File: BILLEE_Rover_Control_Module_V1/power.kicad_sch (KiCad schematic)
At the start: 76 parts, among them CN2 XT60PW-M, U10 +22.2V_POE_POWER, U2 TPS1HA08BQPWPRQ1, U20 +12V_NET_SW_PWR, U23 TPS1HA08BQPWPRQ1, U24 LT8612EUDE#TRPBF, U25 +12V_AUX_PWR, U38 MCP9808T-E/MS, U5 TPS1HA08BQPWPRQ1, U6 INA780BIDEKR, U7 LT8612EUDE#TRPBF, U8 LT8612EUDE#TRPBF, U9 +20V_JETSON_PWR

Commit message: more goodies
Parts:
- removed CN2: XT60PW-M, PDB_LCSC:CONN-TH_XT60PW-M, symbol PDB_LCSC_Libs:XT60PW-M
- added CN1: XT90PW-M.G.Y, PDB_LCSC:CONN-TH_XT90PW-M.G.Y, symbol PDB_LCSC_Libs:XT90PW-M.G.Y
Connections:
- net +22.2V_LOGIC: now also CN1.1 (+)
- net GND: now also CN1.2 (-), CN1.3, CN1.4
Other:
- note added: "Logic XT-90"
- note removed: "Logic XT-60"
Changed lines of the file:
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@@
 		)
 	)
-	(text "Logic XT-60"
+	(text "Logic XT-90"
 		(exclude_from_sim no)
 		(at 14.224 20.828 0)
@@
 	)
 	(junction
-		(at 46.99 36.83)
-		(diameter 0)
-		(color 0 0 0 0)
-	)
-	(junction
 		(at 147.32 187.96)
 		(diameter 0)
@@
 	)
 	(junction
-		(at 55.88 36.83)
-		(diameter 0)
-		(color 0 0 0 0)
-	)
-	(junction
 		(at 295.91 41.91)
 		(diameter 0)
@@
 	)
 	(junction
+		(at 49.53 36.83)
+		(diameter 0)
+		(color 0 0 0 0)
+	)
+	(junction
 		(at 316.23 191.77)
 		(diameter 0)
@@
 	)
 	(junction
+		(at 53.34 36.83)
+		(diameter 0)
+		(color 0 0 0 0)
+	)
+	(junction
 		(at 273.05 74.93)
 		(diameter 0)
@@
 	(wire
 		(pts
-			(xy 46.99 31.75) (xy 46.99 36.83)
+			(xy 49.53 31.75) (xy 49.53 36.83)
 		)
 		(stroke
@@
 	(wire
 		(pts
-			(xy 41.91 29.21) (xy 46.99 29.21)
+			(xy 41.91 29.21) (xy 49.53 29.21)
 		)
 		(stroke
@@
 	(wire
 		(pts
-			(xy 58.42 24.13) (xy 58.42 36.83)
+			(xy 49.53 36.83) (xy 53.34 36.83)
 		)
 		(stroke
@@
 	(wire
 		(pts
-			(xy 55.88 36.83) (xy 58.42 36.83)
-		)
-		(stroke
-			(width 0)
-			(type default)
-		)
-	)
-	(wire
-		(pts
 			(xy 220.98 189.23) (xy 241.3 189.23)
 		)
@@
 	(wire
 		(pts
+			(xy 53.34 36.83) (xy 55.88 36.83)
+		)
+		(stroke
+			(width 0)
+			(type default)
+		)
+	)
+	(wire
+		(pts
 			(xy 63.5 125.73) (xy 59.69 125.73)
 		)
@@
 	(wire
 		(pts
-			(xy 46.99 36.83) (xy 55.88 36.83)
-		)
-		(stroke
-			(width 0)
-			(type default)
-		)
-	)
-	(wire
-		(pts
 			(xy 114.3 38.1) (xy 133.35 38.1)
 		)
@@
 	(wire
 		(pts
-			(xy 55.88 24.13) (xy 58.42 24.13)
-		)
-		(stroke
-			(width 0)
-			(type default)
-		)
-	)
-	(wire
-		(pts
 			(xy 237.49 137.16) (xy 255.27 137.16)
 		)
@@
 	)
 	(symbol
-		(lib_name "LT8612EUDE#TRPBF_1")
 		(lib_id "PDB_LCSC_Libs:LT8612EUDE#TRPBF")
 		(at 273.05 203.2 0)
@@
 	)
 	(symbol
+		(lib_id "PDB_LCSC_Libs:XT90PW-M.G.Y")
+		(at 53.34 30.48 0)
+		(unit 1)
+		(body_style 1)
+		(exclude_from_sim no)
+		(in_bom yes)
+		(on_board yes)
+		(in_pos_files yes)
+		(dnp no)
+		(fields_autoplaced yes)
+		(property "Reference" "CN1"
+			(at 58.42 29.2099 0)
+			(show_name no)
+			(do_not_autoplace no)
+			(effects
+				(font
+					(size 1.27 1.27)
+				)
+				(justify left)
+			)
+		)
+		(property "Value" "XT90PW-M.G.Y"
+			(at 58.42 31.7499 0)
+			(show_name no)
+			(do_not_autoplace no)
+			(effects
+				(font
+					(size 1.27 1.27)
+				)
+				(justify left)
+			)
+		)
+		(property "Footprint" "PDB_LCSC:CONN-TH_XT90PW-M.G.Y"
+			(at 53.34 44.45 0)
+			(hide yes)
+			(show_name no)
+			(do_not_autoplace no)
+			(effects
+				(font
+					(size 1.27 1.27)
+				)
+			)
+		)
+		(property "Datasheet" "https://www.lcsc.com/datasheet/C3040689.pdf"
+			(at 53.34 46.99 0)
+			(hide yes)
+			(show_name no)
+			(do_not_autoplace no)
+			(effects
+				(font
+					(size 1.27 1.27)
+				)
+			)
+		)
+		(property "Description" ""
+			(at 53.34 30.48 0)
+			(hide yes)
+			(show_name no)
+			(do_not_autoplace no)
+			(effects
+				(font
+					(size 1.27 1.27)
+				)
+			)
+		)
+		(property "Manufacturer" "AMASS(艾迈斯)"
+			(at 53.34 49.53 0)
+			(hide yes)
+			(show_name no)
+			(do_not_autoplace no)
+			(effects
+				(font
+					(size 1.27 1.27)
+				)
+			)
+		)
+		(property "MPN" "XT90PW-M.G.Y"
+			(at 53.34 52.07 0)
+			(hide yes)
+			(show_name no)
+			(do_not_autoplace no)
+			(effects
+				(font
+					(size 1.27 1.27)
+				)
+			)
+		)
+		(property "LCSC Part" "C3040689"
+			(at 53.34 54.61 0)
+			(hide yes)
+			(show_name no)
+			(do_not_autoplace no)
+			(effects
+				(font
+					(size 1.27 1.27)
+				)
+			)
+		)
+		(pin "3"
+		)
+		(pin "4"
+		)
+		(pin "1"
+		)
+		(pin "2"
+		)
+		(instances
+			(project "BILLEE_Rover_Control_Module_V1"
+				(path "/e701dc98-f022-461d-84b5-6b2dd8d89d58/e37b5ac2-398e-41bf-8fb6-2ff87cb1df37"
+					(reference "CN1")
+					(unit 1)
+				)
+			)
+		)
+	)
+	(symbol
 		(lib_id "Connector:TestPoint")
 		(at 217.17 115.57 0)
@@
 	(symbol
 		(lib_id "power:PWR_FLAG")
-		(at 46.99 36.83 180)
+		(at 49.53 36.83 180)
 		(unit 1)
 		(body_style 1)
@@
 		(fields_autoplaced yes)
 		(property "Reference" "#FLG03"
-			(at 46.99 38.735 0)
+			(at 49.53 38.735 0)
 			(hide yes)
 			(show_name no)
@@
 		)
 		(property "Value" "PWR_FLAG"
-			(at 46.99 41.91 0)
+			(at 49.53 41.91 0)
 			(show_name no)
 			(do_not_autoplace no)
@@
 		)
 		(property "Footprint" ""
-			(at 46.99 36.83 0)
+			(at 49.53 36.83 0)
 			(hide yes)
 			(show_name no)
@@
 		)
 		(property "Datasheet" ""
-			(at 46.99 36.83 0)
+			(at 49.53 36.83 0)
 			(hide yes)
 			(show_name no)
@@
 		)
 		(property "Description" "Special symbol for telling ERC where power comes from"
-			(at 46.99 36.83 0)
+			(at 49.53 36.83 0)
 			(hide yes)
 			(show_name no)
@@
 	)
 	(symbol
-		(lib_id "PDB_LCSC_Libs:XT60PW-M")
-		(at 52.07 30.48 0)
-		(mirror x)
-		(unit 1)
-		(body_style 1)
-		(exclude_from_sim no)
-		(in_bom yes)
-		(on_board yes)
-		(in_pos_files yes)
-		(dnp no)
-		(property "Reference" "CN2"
-			(at 58.42 31.7501 0)
-			(show_name no)
-			(do_not_autoplace no)
-			(effects
-				(font
-					(size 1.27 1.27)
-				)
-				(justify left)
-			)
-		)
-		(property "Value" "XT60PW-M"
-			(at 58.42 29.2101 0)
-			(show_name no)
-			(do_not_autoplace no)
-			(effects
-				(font
-					(size 1.27 1.27)
-				)
-				(justify left)
-			)
-		)
-		(property "Footprint" "PDB_LCSC:CONN-TH_XT60PW-M"
-			(at 52.07 16.51 0)
-			(hide yes)
-			(show_name no)
-			(do_not_autoplace no)
-			(effects
-				(font
-					(size 1.27 1.27)
-				)
-			)
-		)
-		(property "Datasheet" "https://www.lcsc.com/datasheet/C98732.pdf"
-			(at 52.07 13.97 0)
-			(hide yes)
-			(show_name no)
-			(do_not_autoplace no)
-			(effects
-				(font
-					(size 1.27 1.27)
-				)
-			)
-		)
-		(property "Description" ""
-			(at 52.07 30.48 0)
-			(hide yes)
-			(show_name no)
-			(do_not_autoplace no)
-			(effects
-				(font
-					(size 1.27 1.27)
-				)
-			)
-		)
-		(property "Manufacturer" "AMASS(艾迈斯)"
-			(at 52.07 11.43 0)
-			(hide yes)
-			(show_name no)
-			(do_not_autoplace no)
-			(effects
-				(font
-					(size 1.27 1.27)
-				)
-			)
-		)
-		(property "MPN" "XT60PW-M"
-			(at 52.07 8.89 0)
-			(hide yes)
-			(show_name no)
-			(do_not_autoplace no)
-			(effects
-				(font
-					(size 1.27 1.27)
-				)
-			)
-		)
-		(property "LCSC Part" "C98732"
-			(at 52.07 6.35 0)
-			(hide yes)
-			(show_name no)
-			(do_not_autoplace no)
-			(effects
-				(font
-					(size 1.27 1.27)
-				)
-			)
-		)
-		(pin "1"
-		)
-		(pin "2"
-		)
-		(pin "3"
-		)
-		(pin "4"
-		)
-		(instances
-			(project "BILLEE_Rover_Control_Module_V1"
-				(path "/e701dc98-f022-461d-84b5-6b2dd8d89d58/e37b5ac2-398e-41bf-8fb6-2ff87cb1df37"
-					(reference "CN2")
-					(unit 1)
-				)
-			)
-		)
-	)
-	(symbol
 		(lib_id "power:GND")
 		(at 199.39 207.01 0)
@@
 	)
 	(symbol
-		(lib_name "LT8612EUDE#TRPBF_1")
 		(lib_id "PDB_LCSC_Libs:LT8612EUDE#TRPBF")
 		(at 271.78 53.34 0)
@@
 	)
 	(symbol
-		(lib_name "LT8612EUDE#TRPBF_1")
 		(lib_id "PDB_LCSC_Libs:LT8612EUDE#TRPBF")
 		(at 269.24 129.54 0)
@@
 		(in_pos_files yes)
 		(dnp no)
-		(fields_autoplaced yes)
 		(property "Reference" "#PWR010"
 			(at 55.88 43.18 0)
@@
 		)
 		(property "Value" "GND"
-			(at 55.88 41.91 0)
+			(at 59.436 38.608 0)
 			(show_name no)
 			(do_not_autoplace no)
@@
 		)
 		(property "Value" "PWR_FLAG"
-			(at 41.91 33.782 0)
+			(at 35.306 31.496 0)
 			(show_name no)
 			(do_not_autoplace no)

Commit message: Updated for schematic review by claude
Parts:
- added C62, C63, C64: 4.7u, symbol Device:C
- R32, R43, R65: value 1.91M -> 180k
- R36, R44, R66: value 100k -> 10k
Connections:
- net +22.2V_POE_VCC: now also C63.1
- net GND: now also C62.2, C63.2, C64.2
- net at R65.2, TP8.1, U23.6 (VOUT)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: now also C64.1
- net at R32.2, TP2.1, U2.6 (VOUT)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: now also C62.1

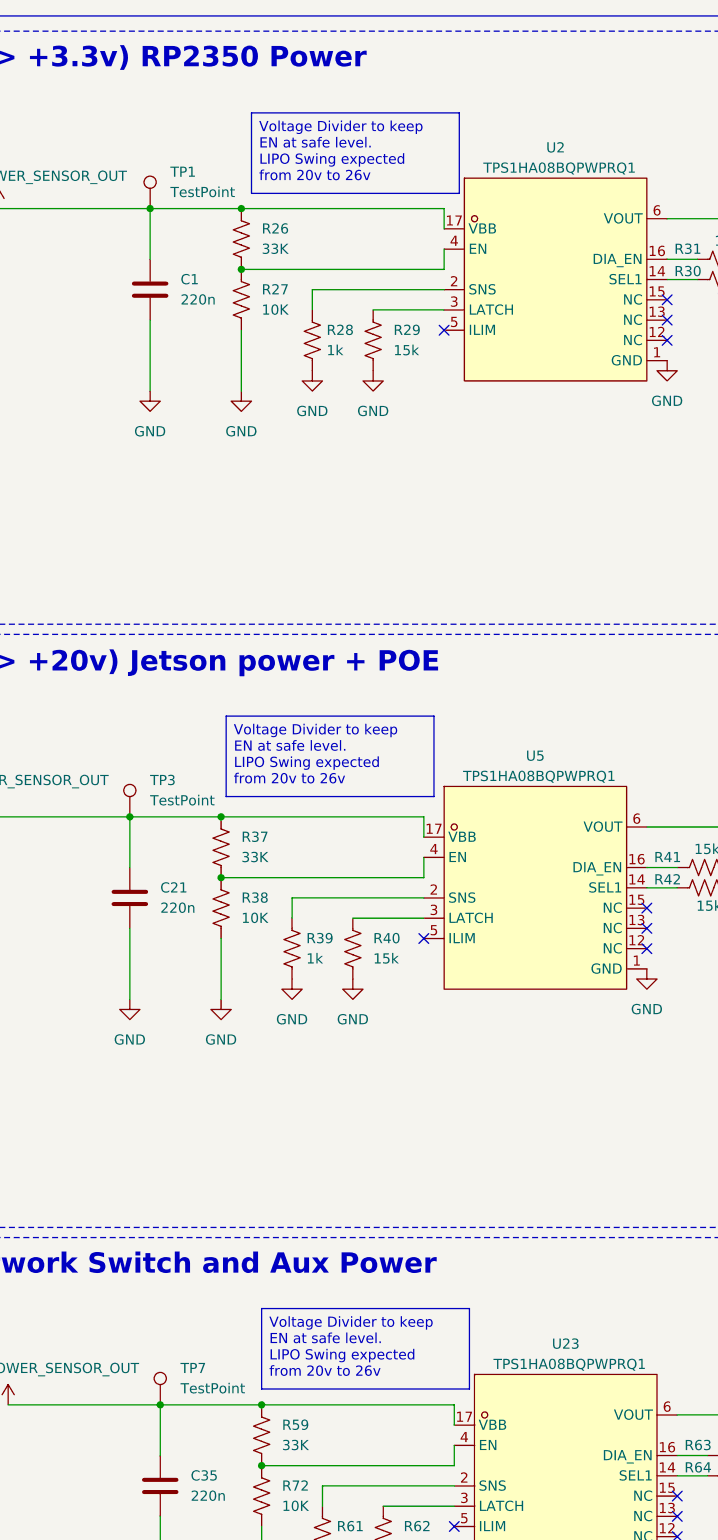
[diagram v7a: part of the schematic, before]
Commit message: Replaced GPIO buffer. Need to add reverse circuit protection. Still trying to figure out what to use
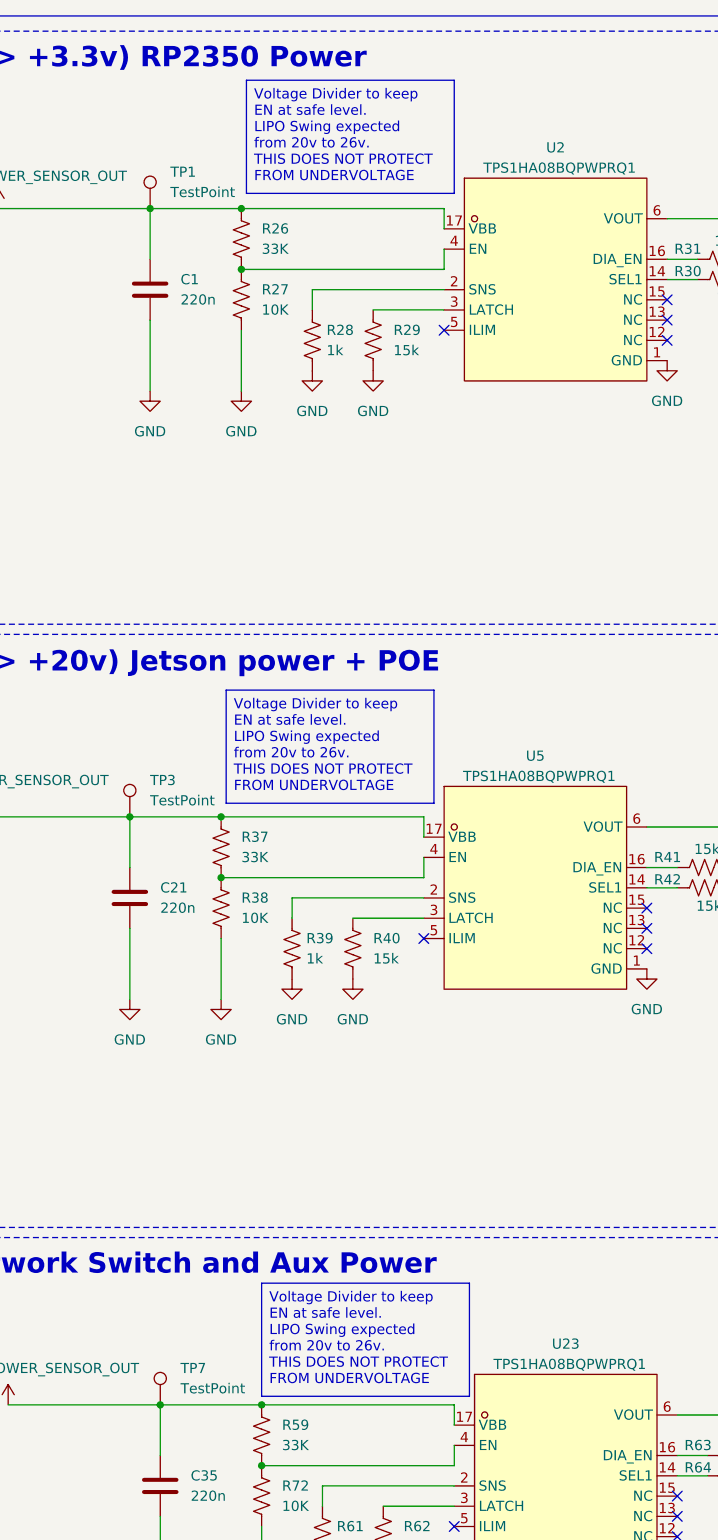
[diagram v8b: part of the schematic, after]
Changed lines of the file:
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@@
 		)
 	)
-	(text_box "Voltage Divider to keep EN at safe level.\nLIPO Swing expected from 20v to 26v"
+	(text_box "Voltage Divider to keep EN at safe level.\nLIPO Swing expected from 20v to 26v.\nTHIS DOES NOT PROTECT FROM UNDERVOLTAGE"
 		(exclude_from_sim no)
-		(at 146.05 26.1128 0)
-		(size 26.035 10.0822)
-		(margins 0.9525 0.9525 0.9525 0.9525)
-		(stroke
-			(width 0)
-			(type solid)
-		)
-		(fill
-			(type none)
-		)
-		(effects
-			(font
-				(size 1.27 1.27)
-			)
-			(justify left top)
-		)
-	)
-	(text_box "Voltage Divider to keep EN at safe level.\nLIPO Swing expected from 20v to 26v"
-		(exclude_from_sim no)
-		(at 142.875 101.6778 0)
-		(size 26.035 10.0822)
+		(at 145.415 22.0236 0)
+		(size 26.035 14.1714)
 		(margins 0.9525 0.9525 0.9525 0.9525)
 		(stroke
@@
 		)
 	)
+	(text_box "Voltage Divider to keep EN at safe level.\nLIPO Swing expected from 20v to 26v.\nTHIS DOES NOT PROTECT FROM UNDERVOLTAGE"
+		(exclude_from_sim no)
+		(at 147.32 172.72 0)
+		(size 26.035 14.1714)
+		(margins 0.9525 0.9525 0.9525 0.9525)
+		(stroke
+			(width 0)
+			(type solid)
+		)
+		(fill
+			(type none)
+		)
+		(effects
+			(font
+				(size 1.27 1.27)
+			)
+			(justify left top)
+		)
+	)
 	(text_box "ADD REVERSE CIRCUIT PROTECTIONSSSSS"
 		(exclude_from_sim no)
@@
 		)
 	)
-	(text_box "Voltage Divider to keep EN at safe level.\nLIPO Swing expected from 20v to 26v"
+	(text_box "Voltage Divider to keep EN at safe level.\nLIPO Swing expected from 20v to 26v.\nTHIS DOES NOT PROTECT FROM UNDERVOLTAGE"
 		(exclude_from_sim no)
-		(at 147.32 175.895 0)
-		(size 26.035 10.0822)
+		(at 142.875 98.425 0)
+		(size 26.035 14.1714)
 		(margins 0.9525 0.9525 0.9525 0.9525)
 		(stroke
